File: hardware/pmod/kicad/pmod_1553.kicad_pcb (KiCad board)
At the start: 2 copper layers, 88.5 x 34.5 mm, 35 parts, among them IC1 TB001-500-02BE, IC2 TB001-500-02BE, J1 Conn_02x06_Top_Bottom, J2 Conn_01x02, J3 Conn_01x02, P1 78604-9JC, P2 78604-9JC, U1 74HC14, U2 VO2630, U3 VO2630

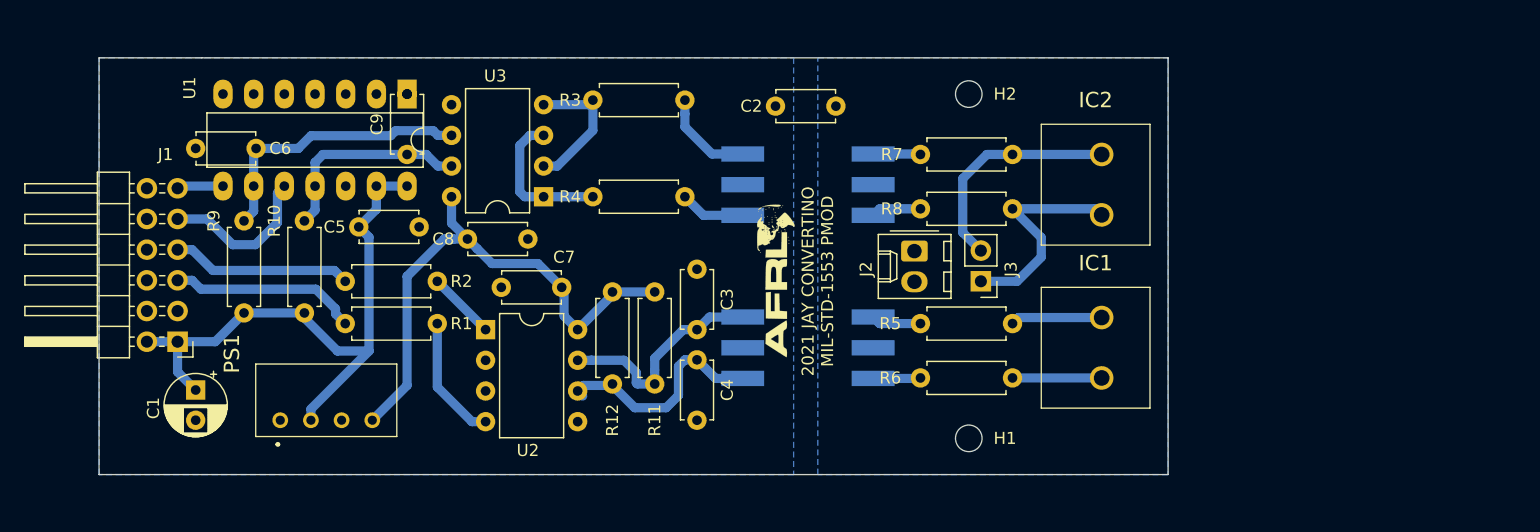
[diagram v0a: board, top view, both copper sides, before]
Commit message: added adg413 switch to pmod1553, added symbols and data sheets for the adg413 and mcp6d11.
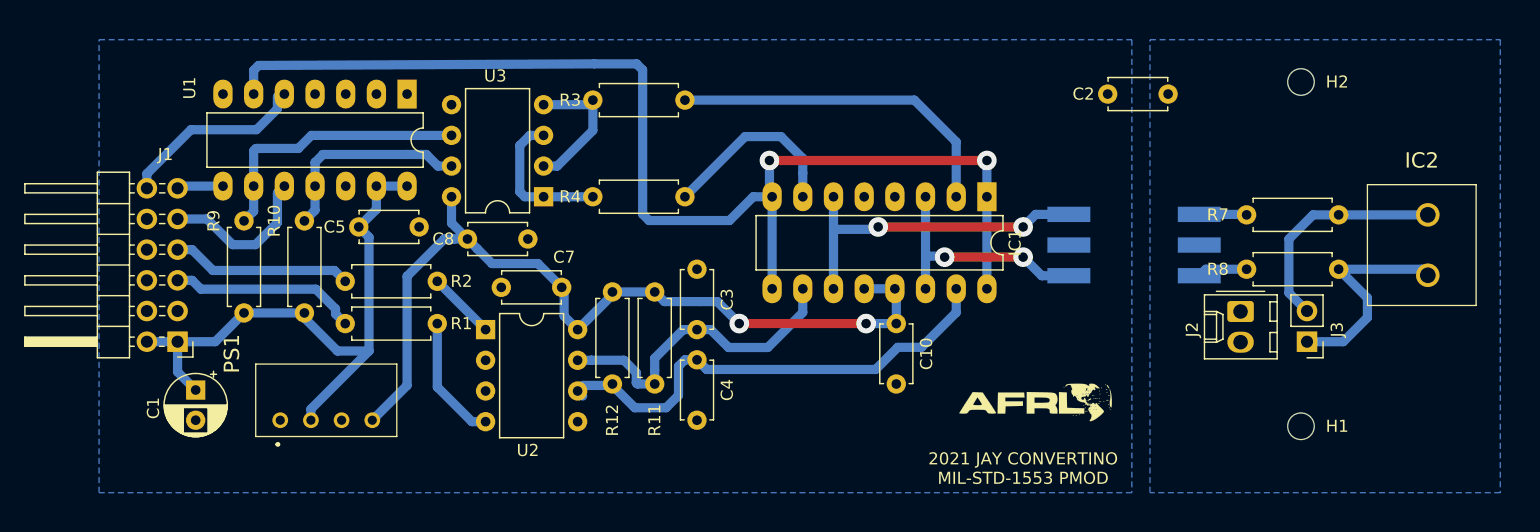
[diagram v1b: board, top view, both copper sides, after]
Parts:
- removed C6, C9: 22pF_DNP, Capacitor_THT:C_Disc_D4.7mm_W2.5mm_P5.00mm
- removed P1: 78604-9JC, murata_pulse_transformers:78604-9JC
- removed R5, R6: 49R9, Resistor_THT:R_Axial_DIN0207_L6.3mm_D2.5mm_P7.62mm_Horizontal
- added C10: 100NF, Capacitor_THT:C_Disc_D4.7mm_W2.5mm_P5.00mm, F.Cu at (160.5, 97.0)
- IC1: value TB001-500-02BE -> ADG413BNZ; footprint cui:TB00150002BE -> Package_DIP:DIP-16_W7.62mm_LongPads
- R10, R9: value 330_2K2-DNP -> 332_2K2-DNP
- moved C2 27.5 mm to (183.0, 78.0)
- moved H1 27.5 mm to (194.0, 105.5)
- moved H2 27.5 mm to (194.0, 77.0)
- moved IC2 27.5 mm to (204.5, 93.0)
- moved J2 27.5 mm to (189.0, 96.0)
- moved J3 27.5 mm to (194.5, 98.5)
- moved P2 27.5 mm to (180.5, 90.5)
- moved R7 27.5 mm to (197.1, 88.0)
- moved R8 27.5 mm to (197.1, 92.5)
- moved L1 23.7 mm to (172.0, 103.5), turned to 0 degrees
- moved IC1 17.8 mm to (168.0, 86.5), turned to 270 degrees
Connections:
- C7 pad 2: Net-(C7-Pad2) -> Net-(C10-Pad1)
- C8 pad 1: Net-(C7-Pad2) -> Net-(C10-Pad1)
- P2 pad 4: Net-(P2-Pad4) -> Net-(IC1-Pad11)
- P2 pad 6: Net-(P2-Pad6) -> Net-(IC1-Pad14)
- PS1 pad 5: Net-(C7-Pad2) -> Net-(C10-Pad1)
- R11 pad 2: Net-(C7-Pad2) -> Net-(C10-Pad1)
- R12 pad 1: Net-(C7-Pad2) -> Net-(C10-Pad1)
- R3 pad 1: Net-(P2-Pad4) -> Net-(IC1-Pad2)
- R4 pad 1: Net-(P2-Pad6) -> Net-(IC1-Pad7)
- U1 pad 5: GNDD -> Net-(J1-Pad12)
- U1 pad 6: Net-(U1-Pad6) -> Net-(IC1-Pad1)
- U2 pad 8: Net-(C7-Pad2) -> Net-(C10-Pad1)
- U3 pad 8: Net-(C7-Pad2) -> Net-(C10-Pad1)
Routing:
- net Net-(IC1-Pad1): track 7.38 -> 97.6 mm, vias 0 -> 2
- net Net-(C10-Pad1): track 0.00 -> 71.4 mm, vias 0 -> 2
- net Net-(C7-Pad2): track 44.6 -> 0.00 mm
- net Net-(IC1-Pad11): track 0.00 -> 27.6 mm, vias 0 -> 2
- net Net-(C4-Pad1): track 19.3 -> 40.5 mm
- net Net-(IC1-Pad2): track 7.59 -> 28.4 mm
- net Net-(IC1-Pad14): track 0.00 -> 20.2 mm, vias 0 -> 2
- net Net-(J1-Pad12): track 0.00 -> 15.9 mm
- net Net-(IC1-Pad7): track 0.00 -> 15.7 mm
- net Net-(C3-Pad2): track 18.5 -> 26.8 mm
- net Net-(P2-Pad4): track 7.93 -> 0.00 mm
- net Net-(P2-Pad6): track 5.42 -> 0.00 mm
- net Net-(P1-Pad1): track 4.14 -> 0.00 mm
- net Net-(P1-Pad3): track 3.99 -> 0.00 mm
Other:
- board outline removed
- net class Default: via_dia 0.8 -> 1.6256; via_drill 0.4 -> 0.7874

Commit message: updated encoder with diff enable line. Added said line to needed cores and projects. Build untested.
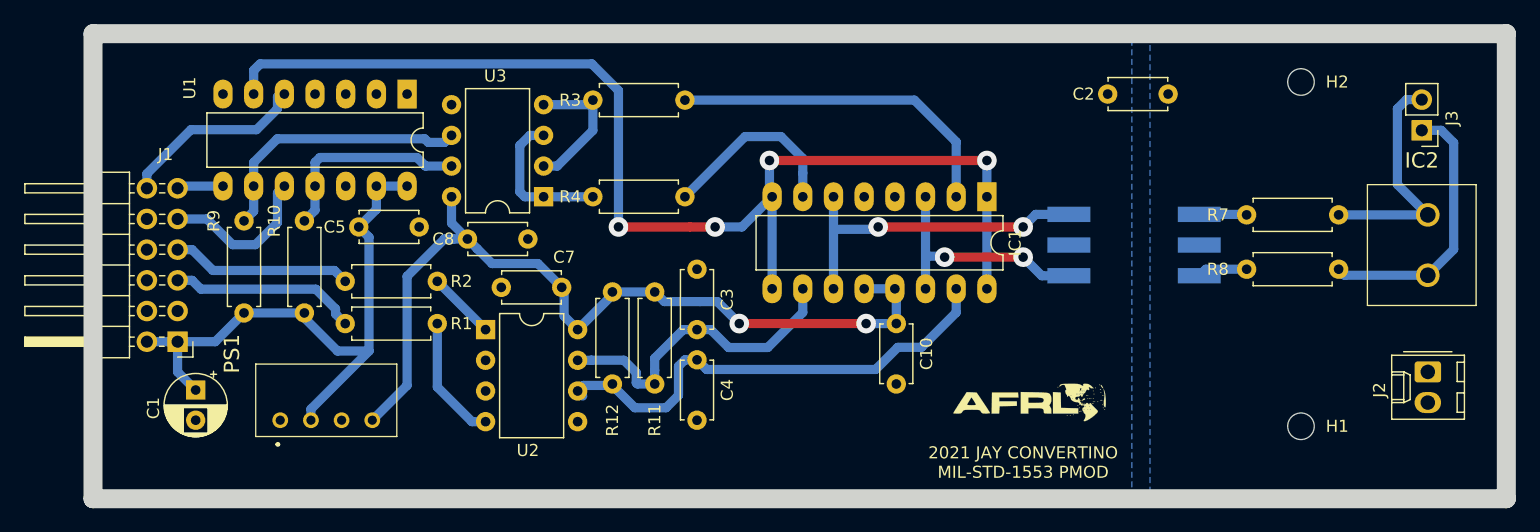
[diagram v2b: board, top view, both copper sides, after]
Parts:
- moved J3 19.9 mm to (204.0, 81.0)
- moved J2 16.3 mm to (204.5, 101.0)
- moved L1 0.50 mm to (171.5, 103.5)
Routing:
- net Net-(IC2-Pad1): track 18.4 -> 22.5 mm
- net Net-(IC1-Pad1): track 97.6 -> 98.3 mm, vias 2 -> 4
- net Net-(IC2-Pad2): track 19.0 -> 19.5 mm
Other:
- board outline added: 117 x 38.5 mm

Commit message: last commit for version 2, updated readme
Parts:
- moved L1 12.3 mm to (177.0, 92.5), turned to 90 degrees
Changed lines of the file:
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@@
   )
   (module logos:afrl (layer F.Cu)
-    (at 171.5 103.5)
-    (fp_text reference L1 (at 0 0) (layer F.SilkS) hide
+    (at 177 92.5 90)
+    (fp_text reference L1 (at 0 0 90) (layer F.SilkS) hide
       (effects (font (size 1.524 1.524) (thickness 0.3)))
     )
-    (fp_text value afrl (at 0.75 0) (layer F.SilkS) hide
+    (fp_text value afrl (at 0.75 0 90) (layer F.SilkS) hide
       (effects (font (size 1.524 1.524) (thickness 0.3)))
     )
@@
   (gr_line (start 94 111.5) (end 211 111.5) (layer Edge.Cuts) (width 1.5748))
   (gr_line (start 94 73) (end 94 111.5) (layer Edge.Cuts) (width 1.5748))
-  (gr_text "2021 JAY CONVERTINO\nMIL-STD-1553 PMOD" (at 171 108.5) (layer F.SilkS)
+  (gr_text "2021 JAY CONVERTINO\nMIL-STD-1553 PMOD" (at 180 92 90) (layer F.SilkS)
     (effects (font (size 1 1) (thickness 0.15)))
   )
